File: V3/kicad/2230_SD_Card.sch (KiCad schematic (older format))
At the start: 9 parts, among them J2210 Micro_SD_Card_Det, U1 74LS07, U2 LP2985-3.3, U2210 74LS07

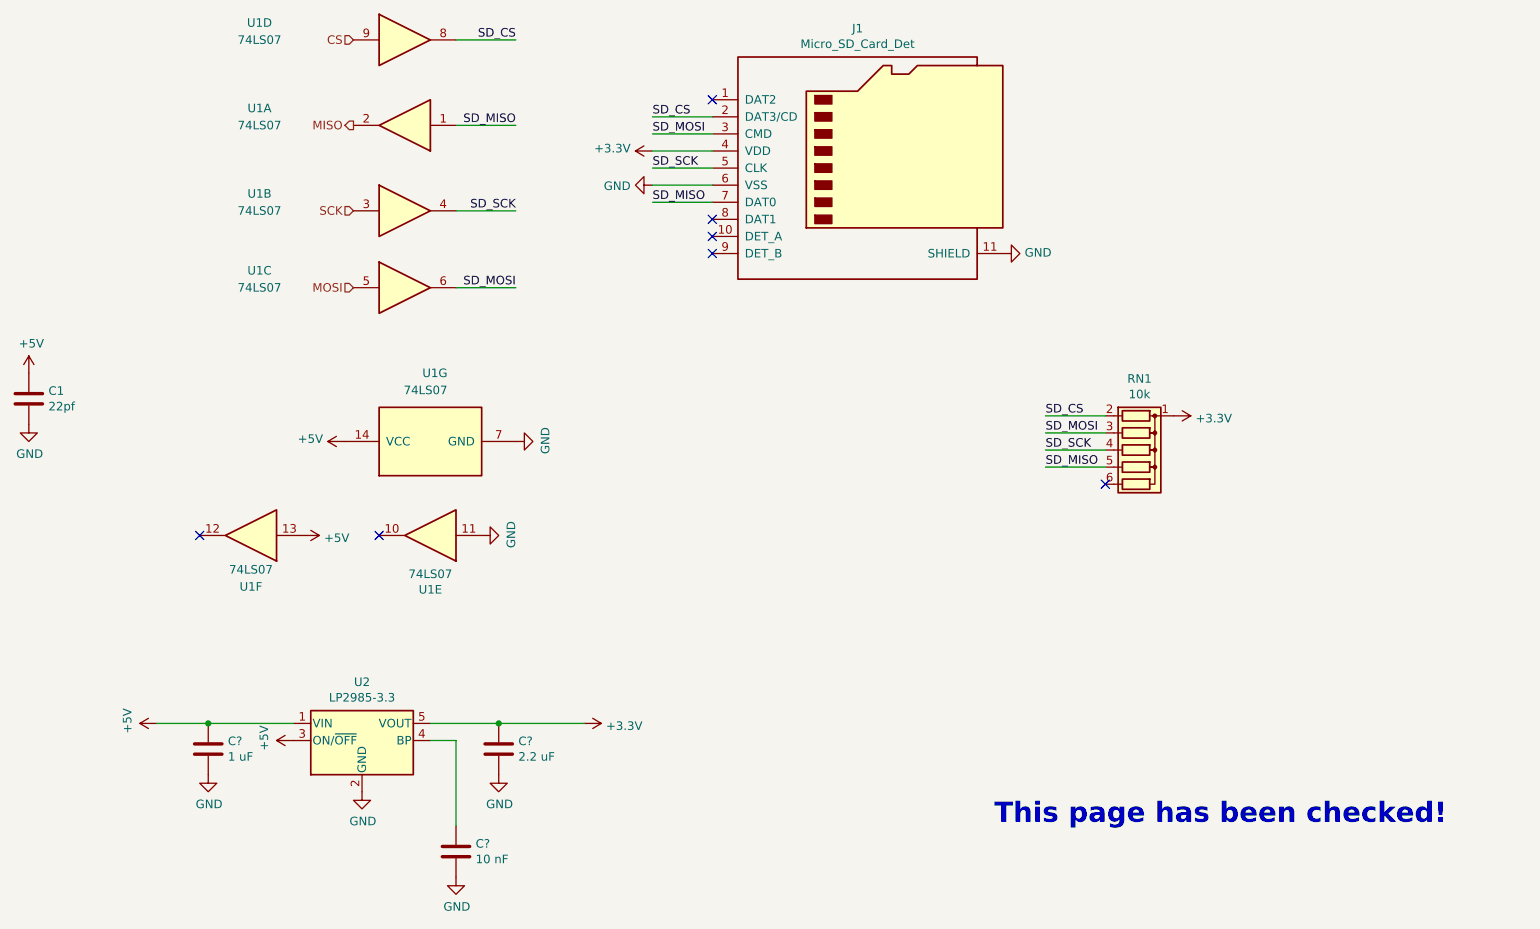
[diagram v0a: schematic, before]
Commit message: 3.1 CSIO SPI Bus (#9)
* Updated SPI to use CPU signals

8 bit register chip controls CS lines

* Renamed and added caps to SD page

* Cleanup
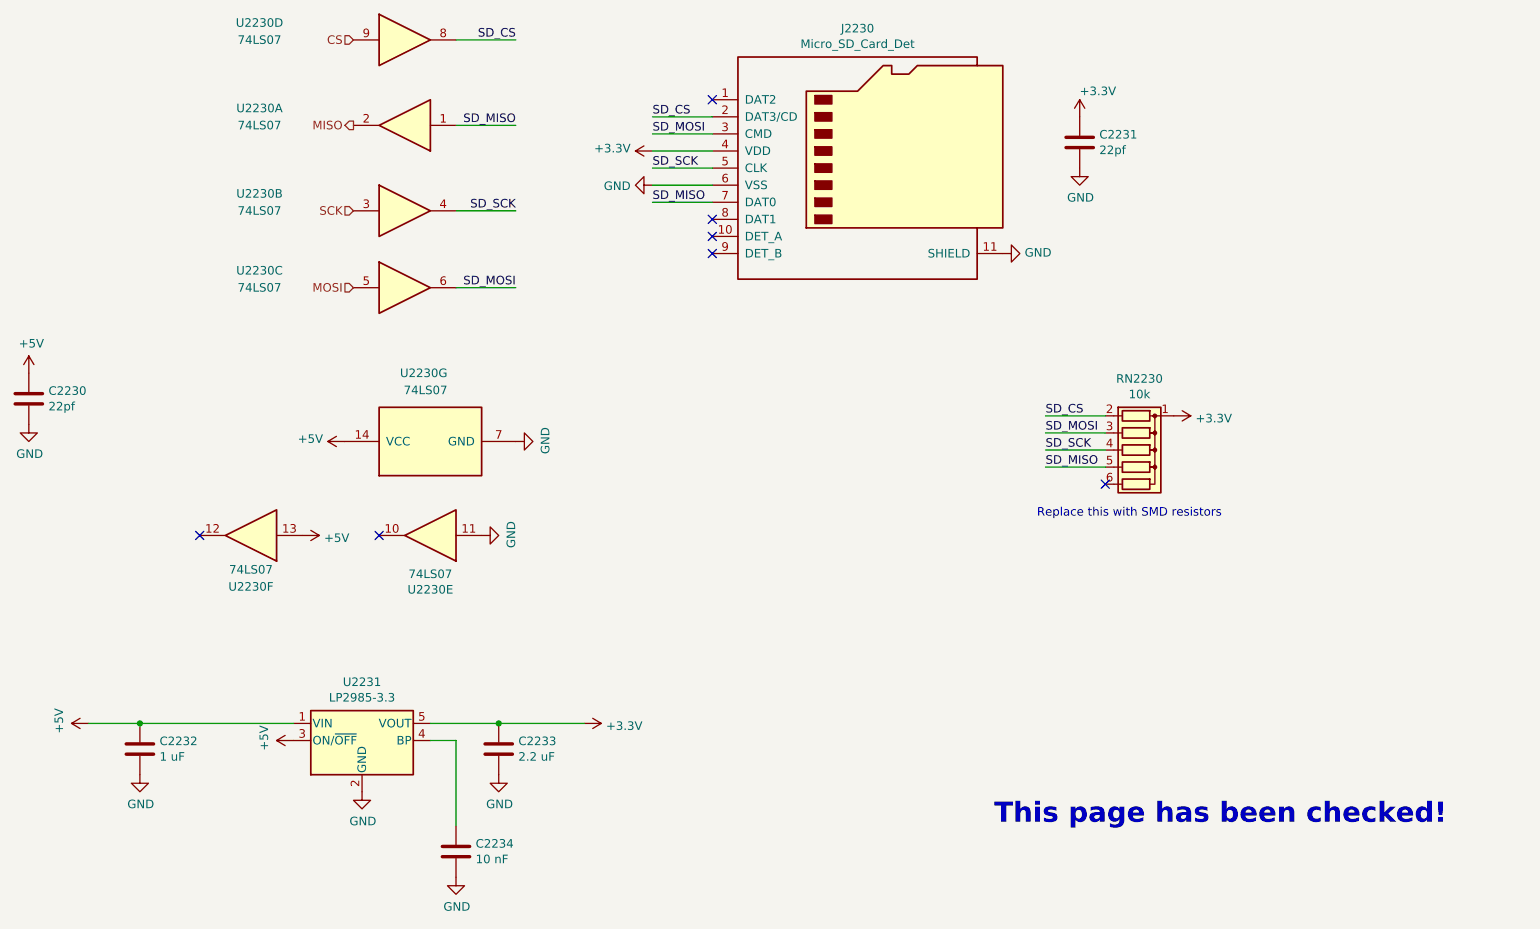
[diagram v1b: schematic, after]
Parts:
- added C2231: 22pf, Capacitor_SMD:C_1206_3216Metric, symbol Device:C
- gave numbers to parts that had none: 3
- renumbered RN1 to RN2230, U1 to U2230, U2 to U2231
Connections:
- net +3V3: now also C2231.1
- net GND: now also C2231.2
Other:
- note added: "Replace this with SMD resistors\n"
- moved on the sheet: C2232

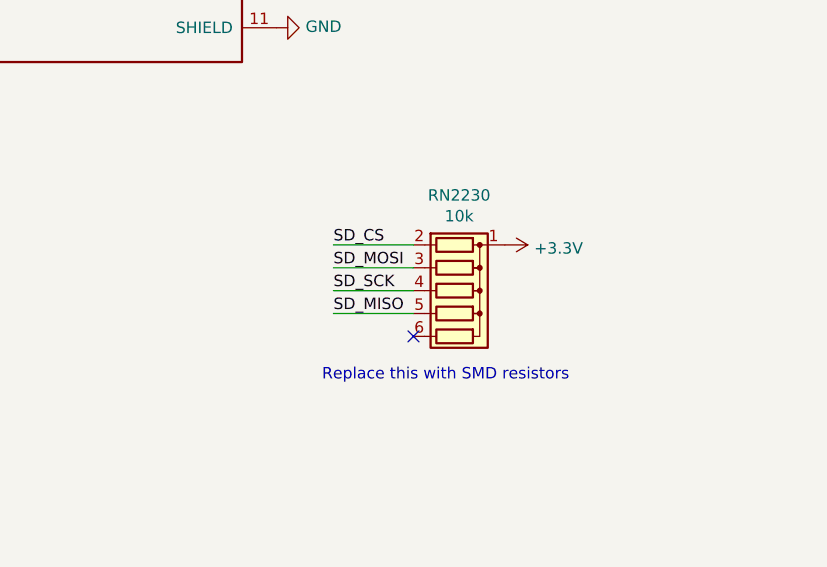
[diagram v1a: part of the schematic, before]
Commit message: First two R arrays
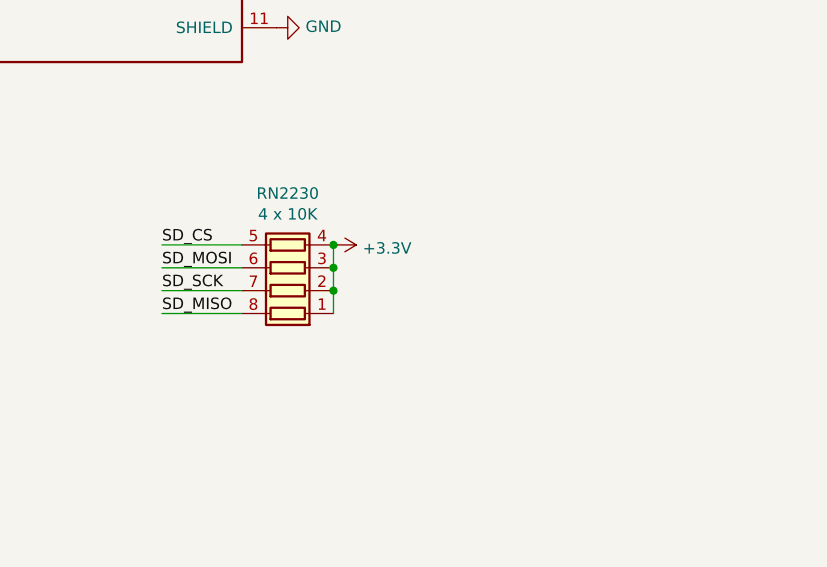
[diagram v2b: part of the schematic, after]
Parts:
- removed RN2230: 10k, Resistor_THT:R_Array_SIP6, symbol Device:R_Network05
- added RN2230: 4 x 10K, Resistor_SMD:R_Array_Convex_4x1206, symbol Device:R_Pack04
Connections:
- net +3V3: now also RN2230.1 (R1.1), RN2230.2 (R2.1), RN2230.3 (R3.1), RN2230.4 (R4.1)
- net SD_CS: now also RN2230.5 (R4.2)
- net SD_MISO: now also RN2230.8 (R1.2)
- net SD_MOSI: now also RN2230.6 (R3.2)
- net SD_SCK: now also RN2230.7 (R2.2)
- no-connect marks 7 -> 6
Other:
- note removed: "Replace this with SMD resistors\n"
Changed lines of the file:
@@
 	0    -1   -1   0
 $EndComp
-Text Label 8100 4700 0    50   ~ 0
+Text Label 7350 4700 0    50   ~ 0
 SD_SCK
-Text Label 8100 4600 0    50   ~ 0
+Text Label 7350 4600 0    50   ~ 0
 SD_MOSI
 Wire Wire Line
-	8100 4700 8450 4700
-Wire Wire Line
-	8100 4600 8450 4600
-Wire Wire Line
-	8450 4500 8100 4500
-Text Label 8100 4500 0    50   ~ 0
+	7350 4700 7700 4700
+Wire Wire Line
+	7350 4600 7700 4600
+Wire Wire Line
+	7700 4500 7350 4500
+Text Label 7350 4500 0    50   ~ 0
 SD_CS
-Text Label 8100 4800 0    50   ~ 0
+Text Label 7350 4800 0    50   ~ 0
 SD_MISO
 Wire Wire Line
-	8100 4800 8450 4800
+	7350 4800 7700 4800
 $Comp
 L power:+3.3V #PWR?
 U 1 1 6259F3FB
-P 8850 4500
+P 8100 4500
 AR Path="/6191B6A2/61F28B7D/6259F3FB" Ref="#PWR?"  Part="1"
 AR Path="/6191B6A2/61F28B7D/62590ED9/6259F3FB" Ref="#PWR0117"  Part="1"
 AR Path="/6191B6A2/61EBDADB/636B5B34/6259F3FB" Ref="#PWR0120"  Part="1"
-F 0 "#PWR0120" H 8850 4350 50  0001 C CNN
-F 1 "+3.3V" V 8865 4628 50  0000 L CNN
-F 2 "" H 8850 4500 50  0001 C CNN
-F 3 "" H 8850 4500 50  0001 C CNN
-	1    8850 4500
+F 0 "#PWR0120" H 8100 4350 50  0001 C CNN
+F 1 "+3.3V" V 8115 4628 50  0000 L CNN
+F 2 "" H 8100 4500 50  0001 C CNN
+F 3 "" H 8100 4500 50  0001 C CNN
+	1    8100 4500
 	0    1    1    0
 $EndComp
@@
 	1    0    0    -1
 $EndComp
-$Comp
-L Device:R_Network05 RN2230
-U 1 1 62618FEB
-P 8650 4700
-F 0 "RN2230" V 8233 4700 50  0000 C CNN
-F 1 "10k" V 8324 4700 50  0000 C CNN
-F 2 "Resistor_THT:R_Array_SIP6" V 9025 4700 50  0001 C CNN
-F 3 "http://www.vishay.com/docs/31509/csc.pdf" H 8650 4700 50  0001 C CNN
-	1    8650 4700
-	0    1    1    0
-$EndComp
 Wire Wire Line
 	5800 3250 6150 3250
@@
 NoConn ~ 6150 3450
 NoConn ~ 6150 3550
-NoConn ~ 8450 4900
 $Comp
 L Regulator_Linear:LP2985-3.3 U2231
@@
 AR Path="/6191B6A2/61F28B7D/63922F7F" Ref="#PWR?"  Part="1"
 AR Path="/6191B6A2/61EBDADB/63922F7F" Ref="#PWR?"  Part="1"
-AR Path="/6191B6A2/61EBDADB/636B5B34/63922F7F" Ref="#PWR?"  Part="1"
-F 0 "#PWR?" H 2800 6350 50  0001 C CNN
+AR Path="/6191B6A2/61EBDADB/636B5B34/63922F7F" Ref="#PWR0159"  Part="1"
+F 0 "#PWR0159" H 2800 6350 50  0001 C CNN
 F 1 "GND" H 2805 6427 50  0000 C CNN
 F 2 "" H 2800 6600 50  0001 C CNN
@@
 AR Path="/6191B6A2/61F28B7D/63926834" Ref="#PWR?"  Part="1"
 AR Path="/6191B6A2/61EBDADB/63926834" Ref="#PWR?"  Part="1"
-AR Path="/6191B6A2/61EBDADB/636B5B34/63926834" Ref="#PWR?"  Part="1"
-F 0 "#PWR?" H 4900 6350 50  0001 C CNN
+AR Path="/6191B6A2/61EBDADB/636B5B34/63926834" Ref="#PWR0163"  Part="1"
+F 0 "#PWR0163" H 4900 6350 50  0001 C CNN
 F 1 "GND" H 4905 6427 50  0000 C CNN
 F 2 "" H 4900 6600 50  0001 C CNN
@@
 AR Path="/6195D2C9/63929039" Ref="#PWR?"  Part="1"
 AR Path="/6191B6A2/61F28B7D/62590ED9/63929039" Ref="#PWR?"  Part="1"
-AR Path="/6191B6A2/61EBDADB/636B5B34/63929039" Ref="#PWR?"  Part="1"
-F 0 "#PWR?" H 3700 6250 50  0001 C CNN
+AR Path="/6191B6A2/61EBDADB/636B5B34/63929039" Ref="#PWR0166"  Part="1"
+F 0 "#PWR0166" H 3700 6250 50  0001 C CNN
 F 1 "+5V" H 3715 6573 50  0000 C CNN
 F 2 "" H 3700 6400 50  0001 C CNN
@@
 AR Path="/6191B6A2/61F28B7D/6392A4D5" Ref="#PWR?"  Part="1"
 AR Path="/6191B6A2/61EBDADB/6392A4D5" Ref="#PWR?"  Part="1"
-AR Path="/6191B6A2/61EBDADB/636B5B34/6392A4D5" Ref="#PWR?"  Part="1"
-F 0 "#PWR?" H 4650 6950 50  0001 C CNN
+AR Path="/6191B6A2/61EBDADB/636B5B34/6392A4D5" Ref="#PWR0167"  Part="1"
+F 0 "#PWR0167" H 4650 6950 50  0001 C CNN
 F 1 "GND" H 4655 7027 50  0000 C CNN
 F 2 "" H 4650 7200 50  0001 C CNN
@@
 Wire Wire Line
 	4650 6400 4650 6900
-Text Notes 8050 5100 0    50   ~ 0
-Replace this with SMD resistors\n
 $Comp
 L Device:C C?
@@
 AR Path="/6195D2C9/63932C3D" Ref="#PWR?"  Part="1"
 AR Path="/6191B6A2/61F28B7D/62590ED9/63932C3D" Ref="#PWR?"  Part="1"
-AR Path="/6191B6A2/61EBDADB/636B5B34/63932C3D" Ref="#PWR?"  Part="1"
-F 0 "#PWR?" H 8300 2800 50  0001 C CNN
+AR Path="/6191B6A2/61EBDADB/636B5B34/63932C3D" Ref="#PWR0170"  Part="1"
+F 0 "#PWR0170" H 8300 2800 50  0001 C CNN
 F 1 "GND" H 8305 2877 50  0000 C CNN
 F 2 "" H 8300 3050 50  0001 C CNN
@@
 AR Path="/6191B6A2/61F28B7D/63933B58" Ref="#PWR?"  Part="1"
 AR Path="/6191B6A2/61F28B7D/62590ED9/63933B58" Ref="#PWR?"  Part="1"
-AR Path="/6191B6A2/61EBDADB/636B5B34/63933B58" Ref="#PWR?"  Part="1"
-F 0 "#PWR?" H 8300 2600 50  0001 C CNN
+AR Path="/6191B6A2/61EBDADB/636B5B34/63933B58" Ref="#PWR0173"  Part="1"
+F 0 "#PWR0173" H 8300 2600 50  0001 C CNN
 F 1 "+3.3V" H 8300 2900 50  0000 L CNN
 F 2 "" H 8300 2750 50  0001 C CNN
@@
 Wire Wire Line
 	2800 6300 3700 6300
+$Comp
+L Device:R_Pack04 RN2230
+U 1 1 6395EBF3
+P 7900 4600
+F 0 "RN2230" V 8225 4600 50  0000 C CNN
+F 1 "4 x 10K" V 8134 4600 50  0000 C CNN
+F 2 "Resistor_SMD:R_Array_Convex_4x1206" V 8175 4600 50  0001 C CNN
+F 3 "~" H 7900 4600 50  0001 C CNN
+	1    7900 4600
+	0    -1   -1   0
+$EndComp
+Wire Wire Line
+	8100 4800 8100 4700
+Connection ~ 8100 4500
+Connection ~ 8100 4600
+Wire Wire Line
+	8100 4600 8100 4500
+Connection ~ 8100 4700
+Wire Wire Line
+	8100 4700 8100 4600
 $EndSCHEMATC

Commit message: Added one more r array
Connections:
- net SD_CS: now also RN2230.8 (R1.2); no longer RN2230.5 (R4.2)
- net SD_MISO: now also RN2230.5 (R4.2); no longer RN2230.8 (R1.2)
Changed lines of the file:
@@
 	7350 4600 7700 4600
 Wire Wire Line
-	7700 4500 7350 4500
+	7700 4800 7350 4800
+Text Label 7350 4800 0    50   ~ 0
+SD_CS
 Text Label 7350 4500 0    50   ~ 0
-SD_CS
-Text Label 7350 4800 0    50   ~ 0
 SD_MISO
 Wire Wire Line
-	7350 4800 7700 4800
+	7350 4500 7700 4500
 $Comp
 L power:+3.3V #PWR?
